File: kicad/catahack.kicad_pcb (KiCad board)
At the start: 4 copper layers, 100 x 100 mm, 175 parts, among them J1 XCVR power choice, J10 PC_AUDIO_EXTRA, J11 Jack header, J12 Jack header, J13 L/R channel choice, J14 Jack header, J15 CITA/OMTP choice, J16 TRRS/TRS+TS choice, J18 Xcvr grounding jumpers, J19 XCVR_Audio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

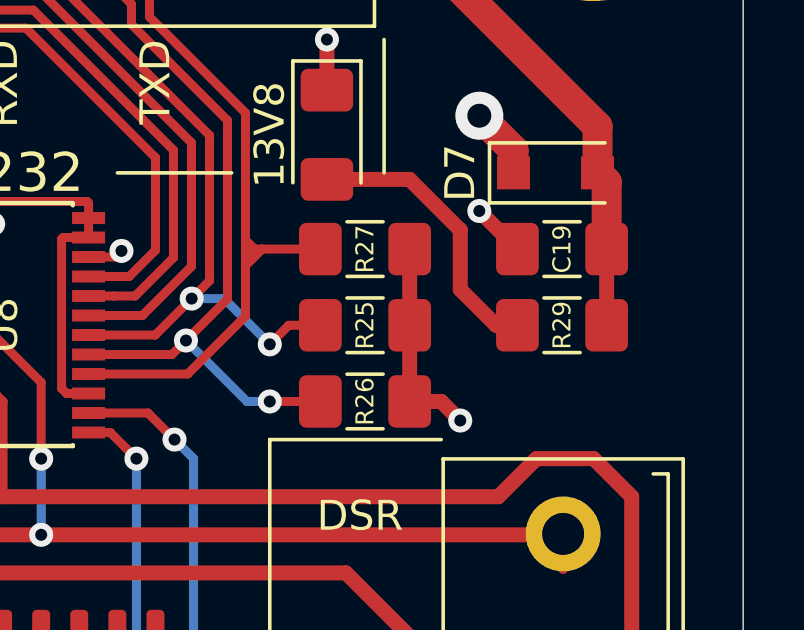
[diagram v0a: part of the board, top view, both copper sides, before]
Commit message: Changed resistor reference location and size; changed gitignore to include gerber dir
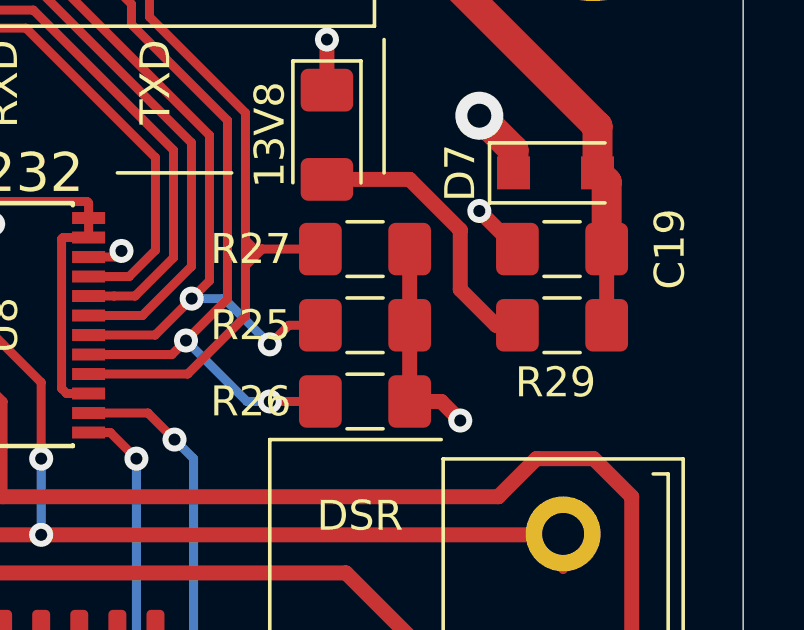
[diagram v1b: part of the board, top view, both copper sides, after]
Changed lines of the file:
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@@
   )
   (setup
-    (last_trace_width 0.5)
+    (last_trace_width 0.3)
     (user_trace_width 0.261)
     (user_trace_width 0.3)
@@
       (padsonsilk false)
       (subtractmaskfromsilk false)
-      (outputformat 4)
+      (outputformat 1)
       (mirror false)
       (drillshape 0)
       (scaleselection 1)
-      (outputdirectory ""))
+      (outputdirectory "gerber/"))
   )
   (net 0 "")
@@
     (tags "resistor handsolder")
     (attr smd)
-    (fp_text reference R25 (at 0 0 270) (layer F.SilkS)
-      (effects (font (size 0.6 0.6) (thickness 0.15)))
+    (fp_text reference R25 (at -3.81 0) (layer F.SilkS)
+      (effects (font (size 1 1) (thickness 0.15)))
     )
     (fp_text value 1k (at 0 1.82) (layer F.Fab)
@@
     (tags "resistor handsolder")
     (attr smd)
-    (fp_text reference R29 (at 0 0 270) (layer F.SilkS)
-      (effects (font (size 0.6 0.6) (thickness 0.15)))
+    (fp_text reference R29 (at 0.2175 -1.905) (layer F.SilkS)
+      (effects (font (size 1 1) (thickness 0.15)))
     )
     (fp_text value 2.2k (at 0 1.82) (layer F.Fab)
@@
     (tags "resistor handsolder")
     (attr smd)
-    (fp_text reference R27 (at 0 0 270) (layer F.SilkS)
-      (effects (font (size 0.6 0.6) (thickness 0.15)))
+    (fp_text reference R27 (at -3.81 0) (layer F.SilkS)
+      (effects (font (size 1 1) (thickness 0.15)))
     )
     (fp_text value 1k (at 0 1.82) (layer F.Fab)
@@
     (tags "capacitor handsolder")
     (attr smd)
-    (fp_text reference C19 (at 0 0 90) (layer F.SilkS)
-      (effects (font (size 0.6 0.6) (thickness 0.15)))
+    (fp_text reference C19 (at -3.5925 0 90) (layer F.SilkS)
+      (effects (font (size 1 1) (thickness 0.15)))
     )
     (fp_text value 100n (at 0 1.82) (layer F.Fab)
@@
     (tags "resistor handsolder")
     (attr smd)
-    (fp_text reference R26 (at 0 0 270) (layer F.SilkS)
-      (effects (font (size 0.6 0.6) (thickness 0.15)))
+    (fp_text reference R26 (at -3.81 0) (layer F.SilkS)
+      (effects (font (size 1 1) (thickness 0.15)))
     )
     (fp_text value 1k (at 0 1.82) (layer F.Fab)
